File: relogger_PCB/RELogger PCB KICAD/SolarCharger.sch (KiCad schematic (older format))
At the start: 21 parts, among them Q2 RFU9110PBF, SW3 ON/OFF, U2 MCP1826S, U3 LM2574, U5 MCP73832

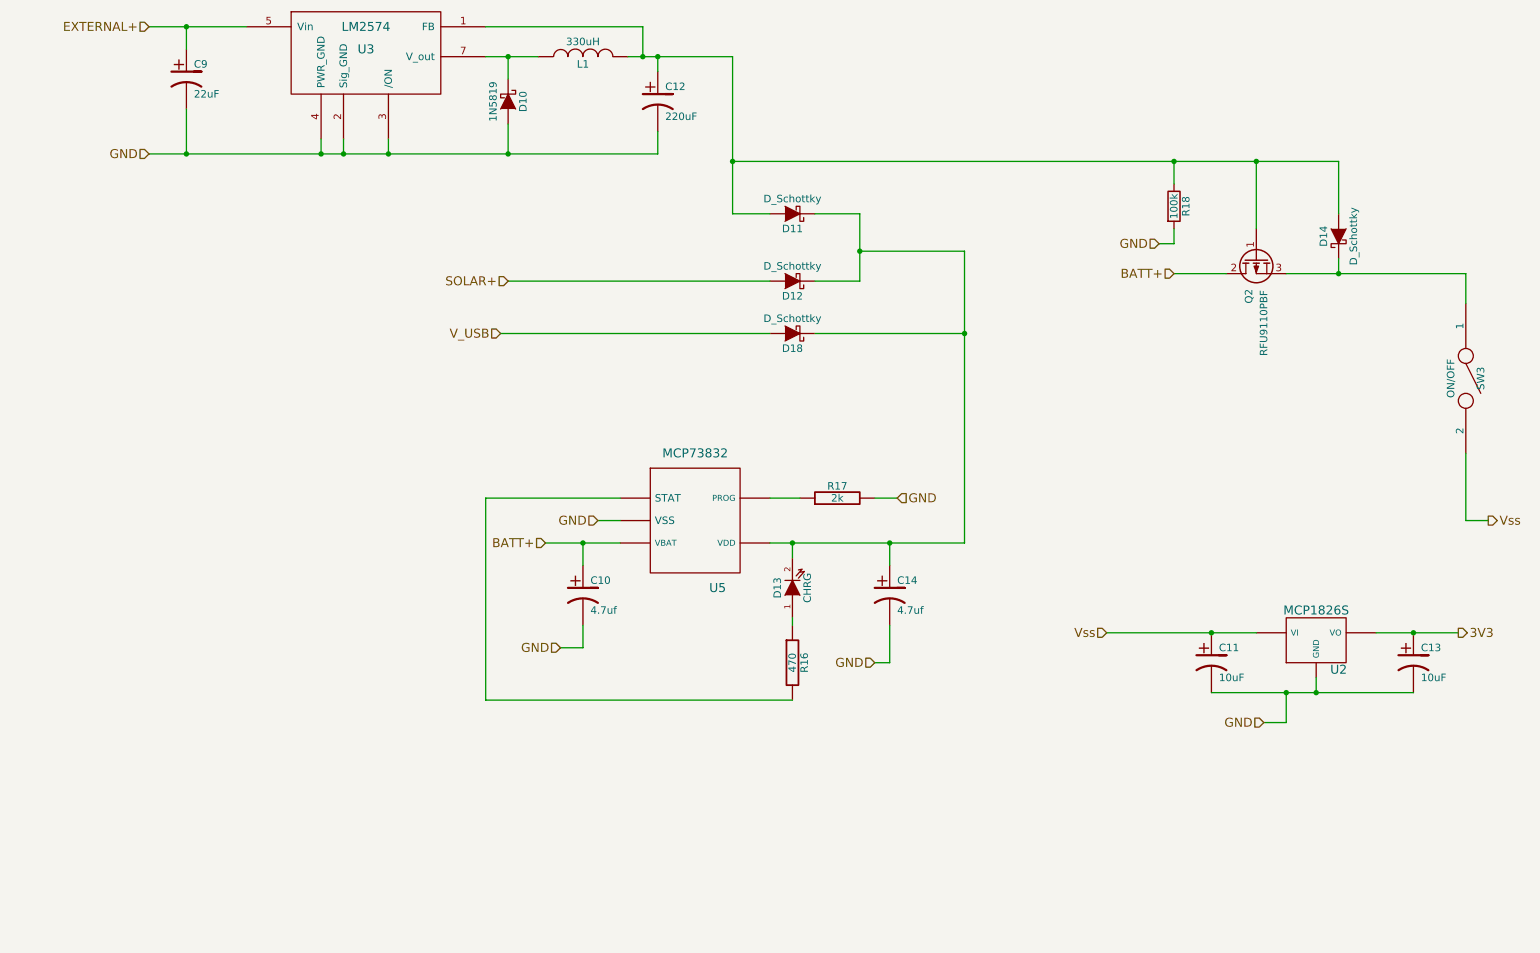
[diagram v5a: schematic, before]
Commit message: Updated new scehmatic.
Still needs Freq conversion circuit. And 3.3V regulator
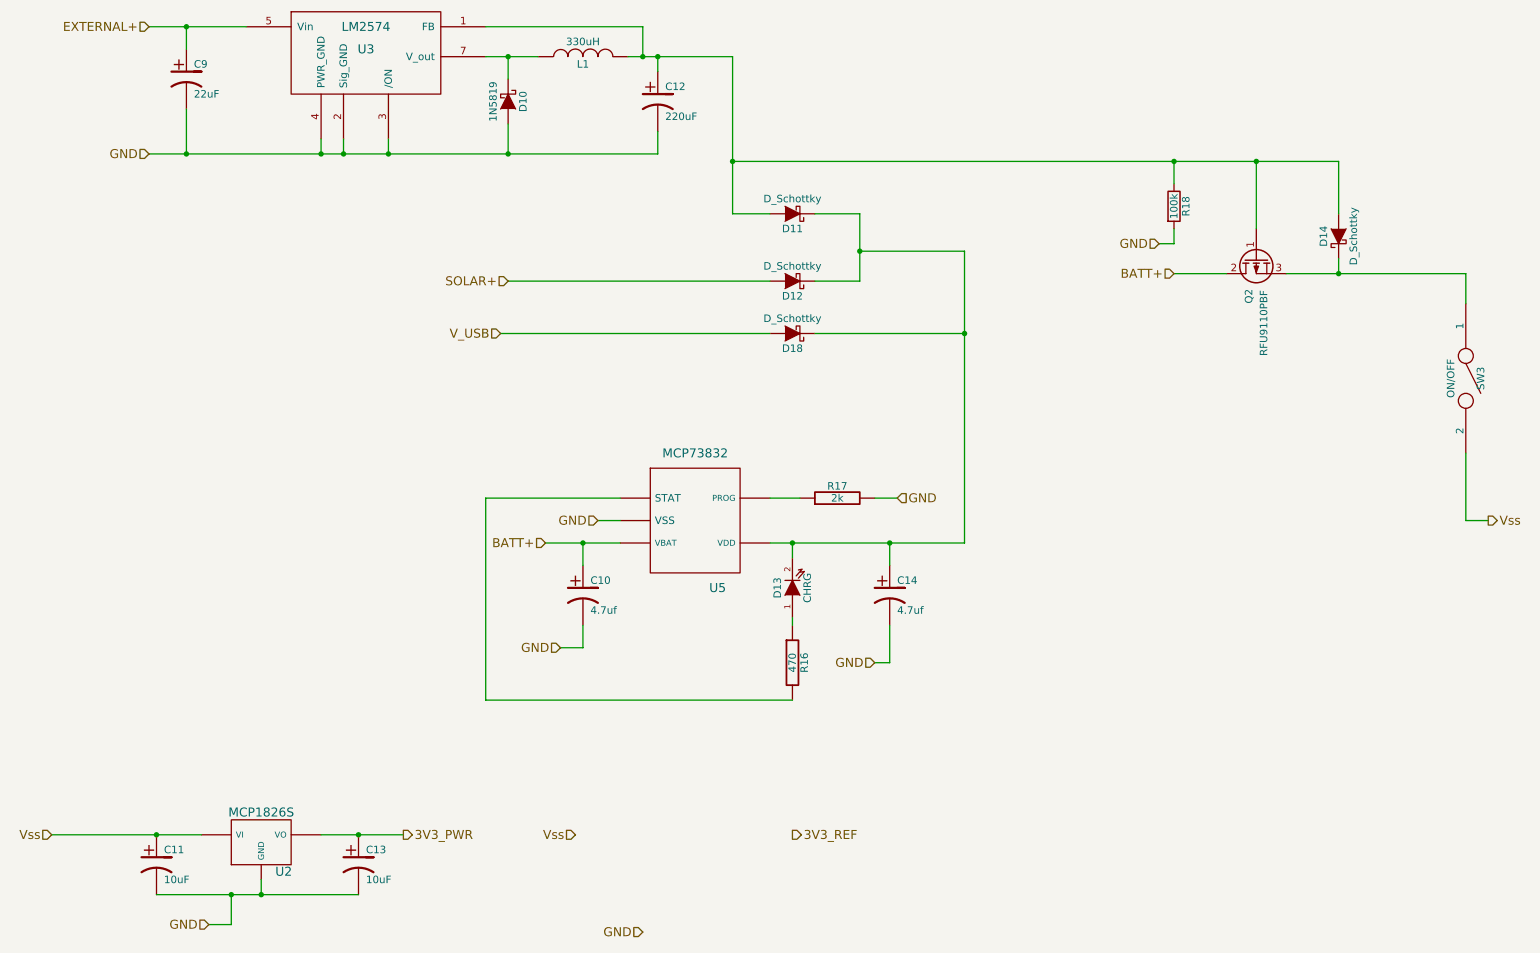
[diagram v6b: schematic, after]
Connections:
- net 3V3 renamed 3V3_PWR
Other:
- moved on the sheet: C11, C13, U2
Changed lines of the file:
@@
 Comment4 ""
 $EndDescr
-Connection ~ 10200 5050
-Wire Wire Line
-	8850 5450 10200 5450
-Connection ~ 8850 5050
+Connection ~ 3150 6400
+Wire Wire Line
+	1800 6800 3150 6800
+Connection ~ 1800 6400
 $Comp
 L CP1-RESCUE-RELogger_PCB_v1 C13
 U 1 1 5463B713
-P 10200 5250
-F 0 "C13" H 10250 5350 50  0000 L CNN
-F 1 "10uF" H 10250 5150 50  0000 L CNN
-F 2 "REInnovationFootprint:C_1V7_TH" H 10200 5250 60  0001 C CNN
-F 3 "" H 10200 5250 60  0001 C CNN
-	1    10200 5250
+P 3150 6600
+F 0 "C13" H 3200 6700 50  0000 L CNN
+F 1 "10uF" H 3200 6500 50  0000 L CNN
+F 2 "REInnovationFootprint:C_1V7_TH" H 3150 6600 60  0001 C CNN
+F 3 "" H 3150 6600 60  0001 C CNN
+	1    3150 6600
 	1    0    0    -1
 $EndComp
@@
 L CP1-RESCUE-RELogger_PCB_v1 C11
 U 1 1 5463B719
-P 8850 5250
-F 0 "C11" H 8900 5350 50  0000 L CNN
-F 1 "10uF" H 8900 5150 50  0000 L CNN
-F 2 "REInnovationFootprint:C_1V7_TH" H 8850 5250 60  0001 C CNN
-F 3 "" H 8850 5250 60  0001 C CNN
-	1    8850 5250
-	1    0    0    -1
-$EndComp
-Text HLabel 10500 5050 2    60   Output ~ 0
-3V3
+P 1800 6600
+F 0 "C11" H 1850 6700 50  0000 L CNN
+F 1 "10uF" H 1850 6500 50  0000 L CNN
+F 2 "REInnovationFootprint:C_1V7_TH" H 1800 6600 60  0001 C CNN
+F 3 "" H 1800 6600 60  0001 C CNN
+	1    1800 6600
+	1    0    0    -1
+$EndComp
+Text HLabel 3450 6400 2    60   Output ~ 0
+3V3_PWR
 Text HLabel 4150 2700 0    60   Input ~ 0
 SOLAR+
@@
 BATT+
 Wire Wire Line
-	9950 5050 10500 5050
+	2900 6400 3450 6400
 Text HLabel 1750 1000 0    60   Input ~ 0
 EXTERNAL+
@@
 Connection ~ 4150 1850
 Wire Wire Line
-	9550 5350 9550 5450
-Connection ~ 9550 5450
-Text HLabel 9200 5650 0    60   Input ~ 0
-GND
-Wire Wire Line
-	9200 5650 9350 5650
-Wire Wire Line
-	9350 5650 9350 5450
-Connection ~ 9350 5450
+	2500 6700 2500 6800
+Connection ~ 2500 6800
+Text HLabel 2150 7000 0    60   Input ~ 0
+GND
+Wire Wire Line
+	2150 7000 2300 7000
+Wire Wire Line
+	2300 7000 2300 6800
+Connection ~ 2300 6800
 Connection ~ 2000 1850
 $Comp
@@
 Text HLabel 4750 4300 0    60   Input ~ 0
 GND
-Text HLabel 8150 5050 0    60   Input ~ 0
+Text HLabel 1100 6400 0    60   Input ~ 0
 Vss
 Text HLabel 4500 5150 0    60   Input ~ 0
@@
 	6200 3050 7200 3050
 Wire Wire Line
-	8150 5050 9150 5050
+	1100 6400 2100 6400
 $Comp
 L MCP1826S U2
 U 1 1 58F214B0
-P 9550 5100
-F 0 "U2" H 9700 4904 60  0000 C CNN
-F 1 "MCP1826S" H 9550 5300 60  0000 C CNN
-F 2 "REInnovationFootprint:TO220_MCP1826S" H 9550 5100 60  0001 C CNN
-F 3 "" H 9550 5100 60  0000 C CNN
-	1    9550 5100
-	1    0    0    -1
-$EndComp
+P 2500 6450
+F 0 "U2" H 2650 6254 60  0000 C CNN
+F 1 "MCP1826S" H 2500 6650 60  0000 C CNN
+F 2 "REInnovationFootprint:TO220_MCP1826S" H 2500 6450 60  0001 C CNN
+F 3 "" H 2500 6450 60  0000 C CNN
+	1    2500 6450
+	1    0    0    -1
+$EndComp
+Text HLabel 6050 6400 2    60   Output ~ 0
+3V3_REF
+Text HLabel 5050 7050 0    60   Input ~ 0
+GND
+Text HLabel 4600 6400 0    60   Input ~ 0
+Vss
 $EndSCHEMATC
